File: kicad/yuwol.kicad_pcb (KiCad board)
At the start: 2 copper layers, 172.5 x 122.5 mm, 120 parts, among them J1 USB_C_Receptacle_PowerOnly_6P, J2 Conn_01x02_Socket, SW1 SW_Push, SW10 SW_Push, SW11 SW_Push, SW12 SW_Push, SW13 SW_Push, SW14 SW_Push, SW15 SW_Push, SW16 SW_Push, SW17 SW_Push, SW18 SW_Push, SW19 SW_Push, SW2 SW_Push, SW20 SW_Push, SW21 SW_Push, SW22 SW_Push, SW23 SW_Push, SW24 SW_Push, SW25 SW_Push, SW26 SW_Push, SW27 SW_Push, SW28 SW_Push, SW29 SW_Push, SW3 SW_Push, SW30 SW_Push, SW31 SW_Push, SW32 SW_Push, SW33 SW_Push, SW34 SW_Push, SW35 SW_Push, SW36 SW_Push, SW37 SW_Push, SW38 SW_Push, SW39 SW_Push, SW4 SW_Push, SW40 SW_Push, SW41 SW_Push, SW42 SW_SPDT, SW5 SW_Push, SW6 SW_Push, SW7 SW_Push, SW8 SW_Push, SW9 SW_Push, U1 ProMicro

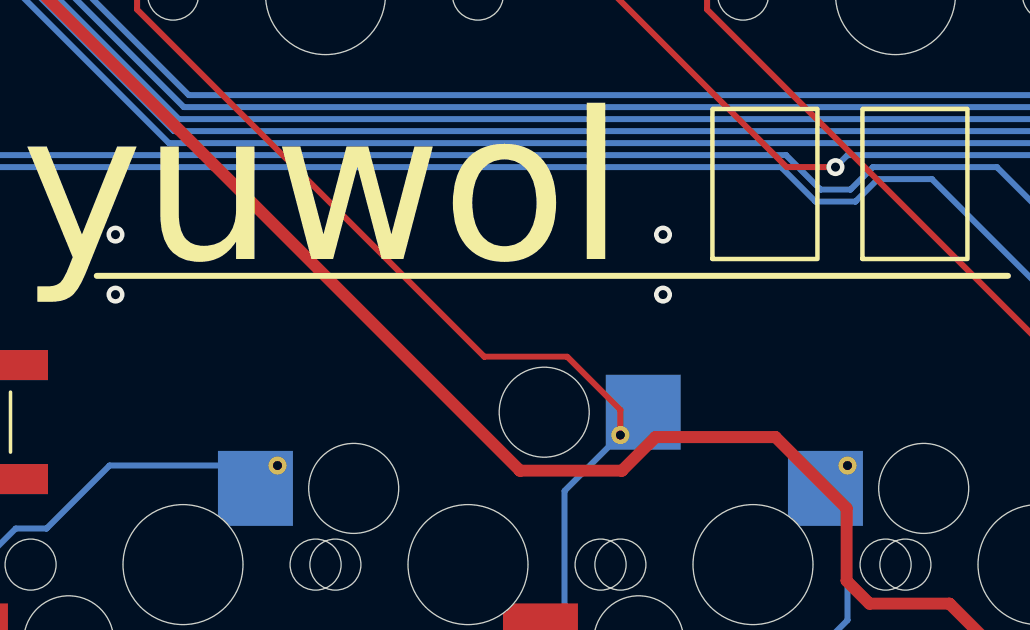
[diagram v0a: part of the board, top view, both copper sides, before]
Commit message: add board point art
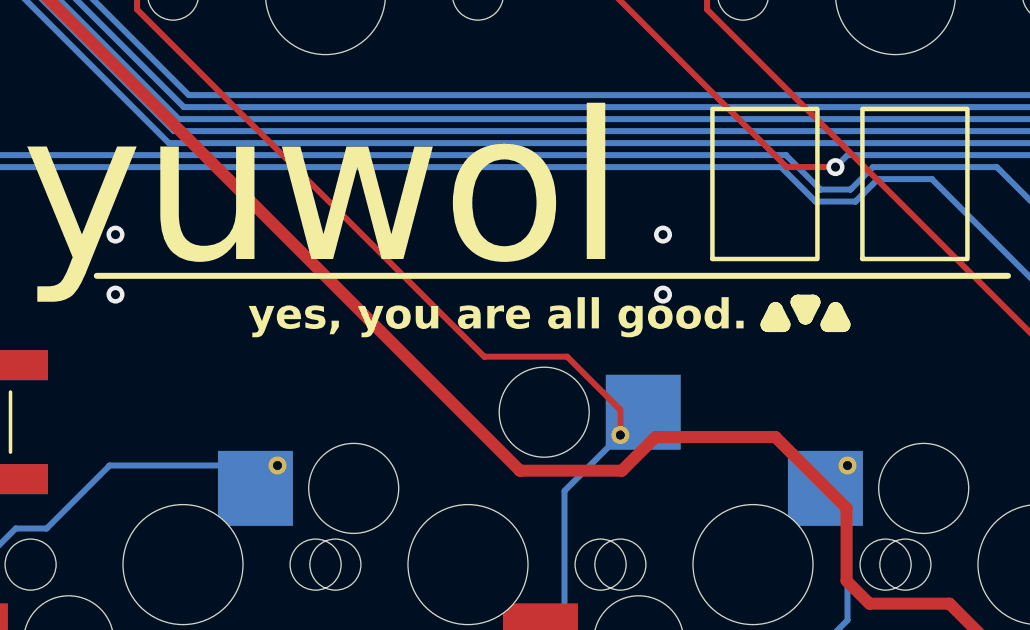
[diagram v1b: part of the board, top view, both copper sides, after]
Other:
- board text added: "yes, you are all good."
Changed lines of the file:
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@@
 		(capping no)
 		(filling no)
-		(zone_defaults)
 		(pcbplotparams
 			(layerselection 0x00000000_00000000_55555555_5755f5ff)
@@
 	)
 	(gr_line
+		(start 133.75 79.5)
+		(end 134.25 79.5)
+		(stroke
+			(width 0.5)
+			(type default)
+		)
+		(layer "F.SilkS")
+	)
+	(gr_line
+		(start 134 79)
+		(end 133.75 79.5)
+		(stroke
+			(width 0.5)
+			(type default)
+		)
+		(layer "F.SilkS")
+	)
+	(gr_line
+		(start 134.25 79.5)
+		(end 134 79)
+		(stroke
+			(width 0.5)
+			(type default)
+		)
+		(layer "F.SilkS")
+	)
+	(gr_line
+		(start 134.75 78.75)
+		(end 135.25 78.75)
+		(stroke
+			(width 0.5)
+			(type default)
+		)
+		(layer "F.SilkS")
+	)
+	(gr_line
+		(start 135 79.25)
+		(end 134.75 78.75)
+		(stroke
+			(width 0.5)
+			(type default)
+		)
+		(layer "F.SilkS")
+	)
+	(gr_line
+		(start 135.25 78.75)
+		(end 135 79.25)
+		(stroke
+			(width 0.5)
+			(type default)
+		)
+		(layer "F.SilkS")
+	)
+	(gr_line
+		(start 135.75 79.5)
+		(end 136.25 79.5)
+		(stroke
+			(width 0.5)
+			(type default)
+		)
+		(layer "F.SilkS")
+	)
+	(gr_line
+		(start 136 79)
+		(end 135.75 79.5)
+		(stroke
+			(width 0.5)
+			(type default)
+		)
+		(layer "F.SilkS")
+	)
+	(gr_line
+		(start 136.25 79.5)
+		(end 136 79)
+		(stroke
+			(width 0.5)
+			(type default)
+		)
+		(layer "F.SilkS")
+	)
+	(gr_line
 		(start 141.75 77.875)
 		(end 111.375 77.875)
@@
 	)
 	(gr_line
+		(start 133.75 79.5)
+		(end 134.25 79.5)
+		(stroke
+			(width 0.5)
+			(type default)
+		)
+		(layer "B.SilkS")
+	)
+	(gr_line
+		(start 134 79)
+		(end 133.75 79.5)
+		(stroke
+			(width 0.5)
+			(type default)
+		)
+		(layer "B.SilkS")
+	)
+	(gr_line
+		(start 134.25 79.5)
+		(end 134 79)
+		(stroke
+			(width 0.5)
+			(type default)
+		)
+		(layer "B.SilkS")
+	)
+	(gr_line
+		(start 134.75 78.75)
+		(end 135.25 78.75)
+		(stroke
+			(width 0.5)
+			(type default)
+		)
+		(layer "B.SilkS")
+	)
+	(gr_line
+		(start 135 79.25)
+		(end 134.75 78.75)
+		(stroke
+			(width 0.5)
+			(type default)
+		)
+		(layer "B.SilkS")
+	)
+	(gr_line
+		(start 135.25 78.75)
+		(end 135 79.25)
+		(stroke
+			(width 0.5)
+			(type default)
+		)
+		(layer "B.SilkS")
+	)
+	(gr_line
+		(start 135.75 79.5)
+		(end 136.25 79.5)
+		(stroke
+			(width 0.5)
+			(type default)
+		)
+		(layer "B.SilkS")
+	)
+	(gr_line
+		(start 136 79)
+		(end 135.75 79.5)
+		(stroke
+			(width 0.5)
+			(type default)
+		)
+		(layer "B.SilkS")
+	)
+	(gr_line
+		(start 136.25 79.5)
+		(end 136 79)
+		(stroke
+			(width 0.5)
+			(type default)
+		)
+		(layer "B.SilkS")
+	)
+	(gr_line
 		(start 142.75 135)
 		(end 69 135)
@@
 		)
 	)
+	(gr_text "yes, you are all good."
+		(at 124.75 79.75 0)
+		(layer "F.SilkS")
+		(effects
+			(font
+				(size 1 1)
+				(thickness 0.2)
+				(bold yes)
+			)
+			(justify bottom)
+		)
+	)
 	(gr_text "yuwol 유월"
 		(at 125 75 0)
@@
 		)
 	)
+	(gr_text "yes, you are all good."
+		(at 124.75 79.75 -0)
+		(layer "B.SilkS")
+		(effects
+			(font
+				(size 1 1)
+				(thickness 0.2)
+				(bold yes)
+			)
+			(justify bottom mirror)
+		)
+	)
 	(gr_text "Jump When\nLEFT SIDE"
 		(at 114.75 117.5 0)
@@
 		)
 	)
+	(group ""
+		(members "01c5d9be-5836-4303-9fce-b2a367091e16" "09daa291-a709-48fb-bc9e-8310c066915b"
+			"10891324-83e6-4e77-810e-83e817eec2af" "12b47f5b-3577-467a-9a6e-9e4aa2b093ca"
+			"150e0c96-afb2-43d6-85ed-4cffc0aebea4" "229edf4c-1051-4aad-9d68-69c93ec81877"
+			"311fdd14-c939-42c8-a4df-1f6edd392191" "38c1bd33-c325-4107-a50b-3fa0188ce65f"
+			"4363c23f-ae3b-4c00-92ba-bc93fb366f95" "4aa79c03-4cb4-44e6-9eb3-c677e760e1cd"
+			"4c46fe11-d153-4061-be44-0d641876ab22" "640da83a-4351-49db-a80f-b1610aea96eb"
+			"7ab730af-b74b-4f9f-bf61-66384ad64143" "980dd158-dbbf-4f3c-abdd-32f98ecb1343"
+			"9bcaf2de-9ea4-43fb-97b4-11ad63b43389" "a357e180-e187-475b-9e53-92265050deb3"
+			"aef1976c-20e8-4f1c-96f9-36d5c1af691d" "b36cc234-3053-4899-84b7-8492f03b5e62"
+			"d6d7a281-cd82-44a6-a468-cde3b06e4ff4" "ee629c81-dd55-4da3-a35a-bfd71d1f1140"
+		)
+	)
